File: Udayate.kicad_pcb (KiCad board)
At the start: 4 copper layers, 60.1 x 60 mm, 113 parts, among them J501 12402012E212A, J502 Conn_01x03_Pin, J503 Conn_01x03_Pin, J504 Conn_01x03_Pin, J505 Conn_01x03_Pin, J506 Conn_01x03_Pin, J507 Conn_01x03_Pin, J508 Conn_01x03_Pin, J509 Conn_01x03_Pin, J601 Conn_01x04_Socket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

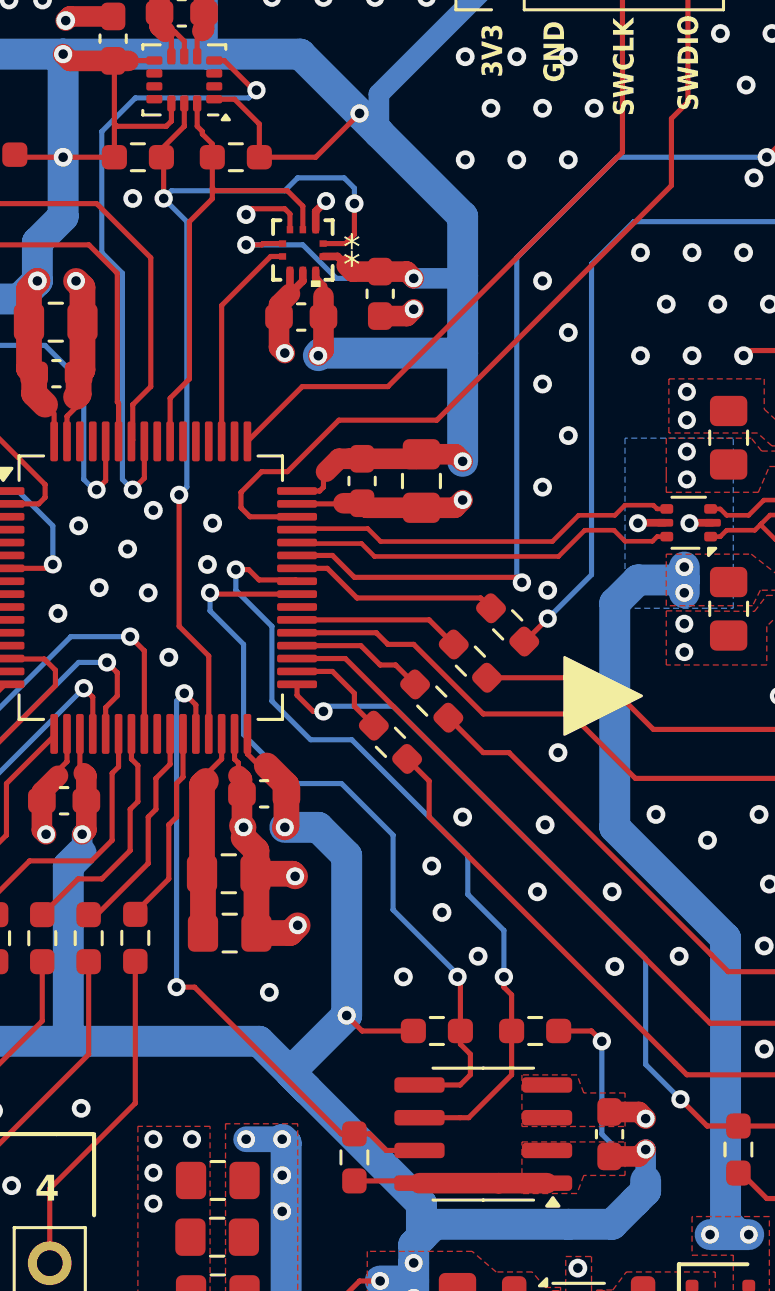
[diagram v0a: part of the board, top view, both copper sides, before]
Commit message: fix: EEPROM WC assigned to PC25
boot1 pull down, DFU now works
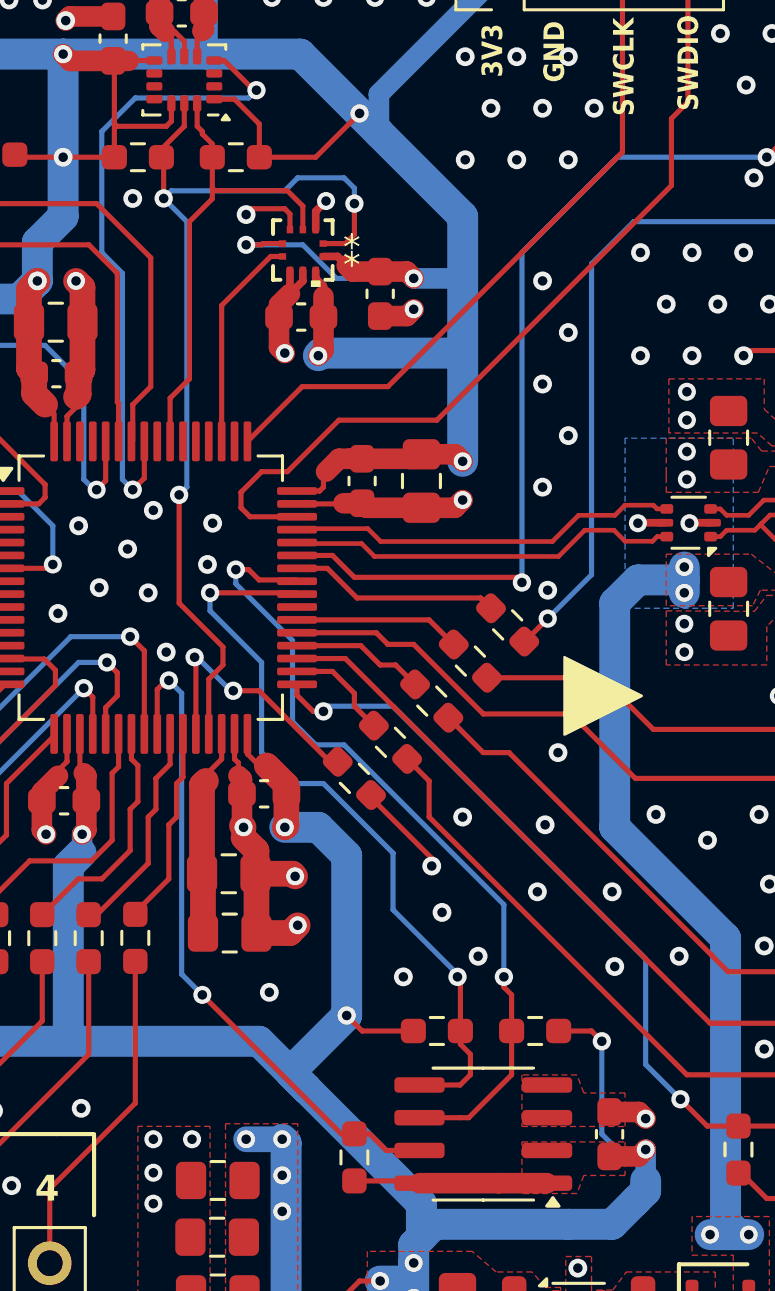
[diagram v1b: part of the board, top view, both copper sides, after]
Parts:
- added R226: 5K1, Resistor_SMD:R_0603_1608Metric_Pad0.98x0.95mm_HandSolder, F.Cu at (153.6, 105.7)
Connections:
- U201 pad 25: unconnected-(U201-PC5-Pad25) -> /MCU/D_M24C02_WC
- U201 pad 28: /MCU/D_M24C02_WC -> /MCU/D_BOOT1
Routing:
- net /MCU/D_BOOT1: track 0.00 -> 10.1 mm, vias 0 -> 2
- net GND: track 148.3 -> 152.1 mm
- net /MCU/D_M24C02_WC: track 25.3 -> 26.0 mm
